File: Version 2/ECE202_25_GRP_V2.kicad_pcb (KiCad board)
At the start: 2 copper layers, 90.2 x 55.1 mm, 27 parts, among them J1 Run_in+, J10 Reverse_in+, J11 ground_in, J12 LED_Low_V+, J2 Brake_in+, J3 Turn_in+, J4 Run_out+, J5 Reverse_Out, J6 Turn_out+, J7 ground_out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

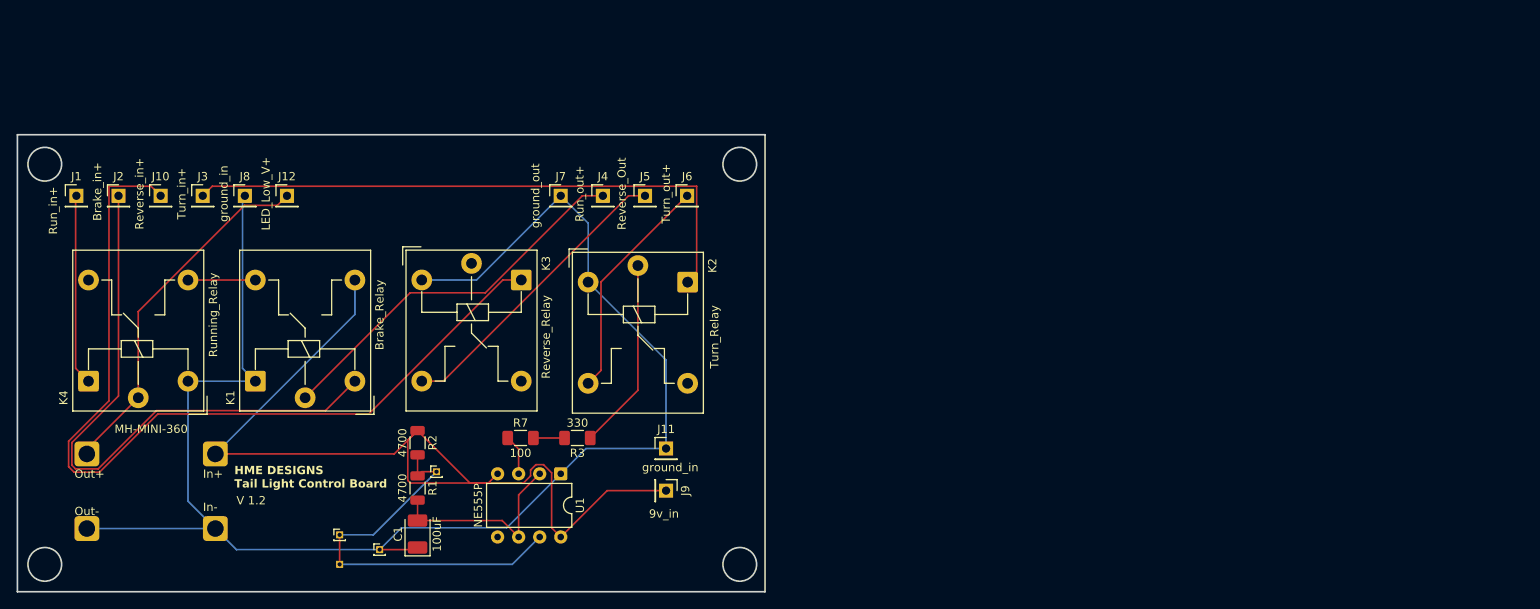
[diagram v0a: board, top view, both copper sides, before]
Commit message: LED Board, practice board, button board updates
Created led board and practice board/business card. Updated mounting for buttons on button board. Submitted all 3 for production on 4/6/25
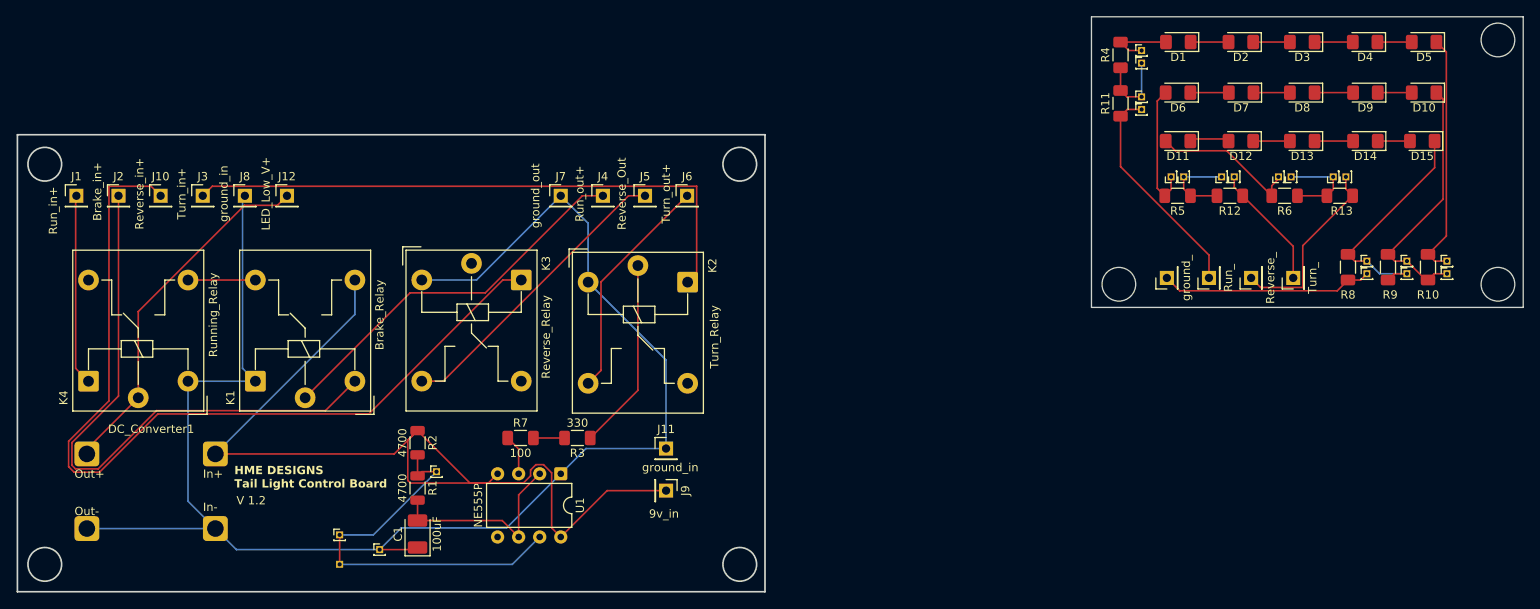
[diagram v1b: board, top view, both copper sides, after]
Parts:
- added D1: LED, LED_SMD:LED_1206_3216Metric_Pad1.42x1.75mm_HandSolder, F.Cu at (228.1, 28.4)
- added D10: LED, LED_SMD:LED_1206_3216Metric_Pad1.42x1.75mm_HandSolder, F.Cu at (257.8, 34.5)
- added D11: LED, LED_SMD:LED_1206_3216Metric_Pad1.42x1.75mm_HandSolder, F.Cu at (228.1, 40.4)
- added D12: LED, LED_SMD:LED_1206_3216Metric_Pad1.42x1.75mm_HandSolder, F.Cu at (235.7, 40.4)
- added D13: LED, LED_SMD:LED_1206_3216Metric_Pad1.42x1.75mm_HandSolder, F.Cu at (243.1, 40.4)
- added D14: LED, LED_SMD:LED_1206_3216Metric_Pad1.42x1.75mm_HandSolder, F.Cu at (250.7, 40.4)
- added D15: LED, LED_SMD:LED_1206_3216Metric_Pad1.42x1.75mm_HandSolder, F.Cu at (257.6, 40.4)
- added D2: LED, LED_SMD:LED_1206_3216Metric_Pad1.42x1.75mm_HandSolder, F.Cu at (235.7, 28.4)
- added D3: LED, LED_SMD:LED_1206_3216Metric_Pad1.42x1.75mm_HandSolder, F.Cu at (243.1, 28.4)
- added D4: LED, LED_SMD:LED_1206_3216Metric_Pad1.42x1.75mm_HandSolder, F.Cu at (250.7, 28.4)
- added D5: LED, LED_SMD:LED_1206_3216Metric_Pad1.42x1.75mm_HandSolder, F.Cu at (257.8, 28.4)
- added D6: LED, LED_SMD:LED_1206_3216Metric_Pad1.42x1.75mm_HandSolder, F.Cu at (228.1, 34.5)
- added D7: LED, LED_SMD:LED_1206_3216Metric_Pad1.42x1.75mm_HandSolder, F.Cu at (235.7, 34.5)
- added D8: LED, LED_SMD:LED_1206_3216Metric_Pad1.42x1.75mm_HandSolder, F.Cu at (243.1, 34.5)
- added D9: LED, LED_SMD:LED_1206_3216Metric_Pad1.42x1.75mm_HandSolder, F.Cu at (250.7, 34.5)
- added J13: Run_, Connector_PinHeader_2.54mm:PinHeader_1x01_P2.54mm_Vertical, F.Cu at (231.8, 56.9)
- added J14: Turn_, Connector_PinHeader_2.54mm:PinHeader_1x01_P2.54mm_Vertical, F.Cu at (242.0, 56.9)
- added J15: Reverse_, Connector_PinHeader_2.54mm:PinHeader_1x01_P2.54mm_Vertical, F.Cu at (236.9, 56.9)
- added J16: ground_, Connector_PinHeader_2.54mm:PinHeader_1x01_P2.54mm_Vertical, F.Cu at (226.8, 56.9)
- added R10: 330, Resistor_SMD:R_1206_3216Metric_Pad1.30x1.75mm_HandSolder, F.Cu at (258.3, 55.6)
- added R11: 330, Resistor_SMD:R_1206_3216Metric_Pad1.30x1.75mm_HandSolder, F.Cu at (221.2, 35.8)
- added R12: 330, Resistor_SMD:R_1206_3216Metric_Pad1.30x1.75mm_HandSolder, F.Cu at (234.4, 47.0)
- added R13: 330, Resistor_SMD:R_1206_3216Metric_Pad1.30x1.75mm_HandSolder, F.Cu at (247.6, 47.0)
- added R4: 330, Resistor_SMD:R_1206_3216Metric_Pad1.30x1.75mm_HandSolder, F.Cu at (221.2, 30.0)
- added R5: 330, Resistor_SMD:R_1206_3216Metric_Pad1.30x1.75mm_HandSolder, F.Cu at (228.1, 47.0)
- added R6: 330, Resistor_SMD:R_1206_3216Metric_Pad1.30x1.75mm_HandSolder, F.Cu at (241.0, 47.0)
- added R8: 330, Resistor_SMD:R_1206_3216Metric_Pad1.30x1.75mm_HandSolder, F.Cu at (248.6, 55.6)
- added R9: 330, Resistor_SMD:R_1206_3216Metric_Pad1.30x1.75mm_HandSolder, F.Cu at (253.4, 55.6)
- added REF**: PinHeader_1x01_P1.00mm_Vertical, Connector_PinHeader_1.00mm:PinHeader_1x01_P1.00mm_Vertical, F.Cu at (255.7, 54.9)
- added REF**: PinHeader_1x01_P1.00mm_Vertical, Connector_PinHeader_1.00mm:PinHeader_1x01_P1.00mm_Vertical, F.Cu at (248.4, 44.7)
- added REF**: PinHeader_1x01_P1.00mm_Vertical, Connector_PinHeader_1.00mm:PinHeader_1x01_P1.00mm_Vertical, F.Cu at (223.7, 35.1)
- added REF**: PinHeader_1x01_P1.00mm_Vertical, Connector_PinHeader_1.00mm:PinHeader_1x01_P1.00mm_Vertical, F.Cu at (234.9, 44.7)
- added REF**: PinHeader_1x01_P1.00mm_Vertical, Connector_PinHeader_1.00mm:PinHeader_1x01_P1.00mm_Vertical, F.Cu at (223.7, 36.6)
- added REF**: PinHeader_1x01_P1.00mm_Vertical, Connector_PinHeader_1.00mm:PinHeader_1x01_P1.00mm_Vertical, F.Cu at (246.8, 44.7)
- added REF**: PinHeader_1x01_P1.00mm_Vertical, Connector_PinHeader_1.00mm:PinHeader_1x01_P1.00mm_Vertical, F.Cu at (260.6, 56.4)
- added REF**: PinHeader_1x01_P1.00mm_Vertical, Connector_PinHeader_1.00mm:PinHeader_1x01_P1.00mm_Vertical, F.Cu at (255.7, 56.4)
- added REF**: PinHeader_1x01_P1.00mm_Vertical, Connector_PinHeader_1.00mm:PinHeader_1x01_P1.00mm_Vertical, F.Cu at (240.2, 44.7)
- added REF**: PinHeader_1x01_P1.00mm_Vertical, Connector_PinHeader_1.00mm:PinHeader_1x01_P1.00mm_Vertical, F.Cu at (223.7, 31.0)
- added REF**: PinHeader_1x01_P1.00mm_Vertical, Connector_PinHeader_1.00mm:PinHeader_1x01_P1.00mm_Vertical, F.Cu at (260.6, 54.9)
- added REF**: PinHeader_1x01_P1.00mm_Vertical, Connector_PinHeader_1.00mm:PinHeader_1x01_P1.00mm_Vertical, F.Cu at (250.9, 56.4)
- added REF**: PinHeader_1x01_P1.00mm_Vertical, Connector_PinHeader_1.00mm:PinHeader_1x01_P1.00mm_Vertical, F.Cu at (250.9, 54.9)
- added REF**: PinHeader_1x01_P1.00mm_Vertical, Connector_PinHeader_1.00mm:PinHeader_1x01_P1.00mm_Vertical, F.Cu at (228.8, 44.7)
- added REF**: PinHeader_1x01_P1.00mm_Vertical, Connector_PinHeader_1.00mm:PinHeader_1x01_P1.00mm_Vertical, F.Cu at (223.7, 29.5)
- added REF**: PinHeader_1x01_P1.00mm_Vertical, Connector_PinHeader_1.00mm:PinHeader_1x01_P1.00mm_Vertical, F.Cu at (233.4, 44.7)
- added REF**: PinHeader_1x01_P1.00mm_Vertical, Connector_PinHeader_1.00mm:PinHeader_1x01_P1.00mm_Vertical, F.Cu at (241.8, 44.7)
- added REF**: PinHeader_1x01_P1.00mm_Vertical, Connector_PinHeader_1.00mm:PinHeader_1x01_P1.00mm_Vertical, F.Cu at (227.3, 44.7)
- renumbered MH-MINI-360 to DC_Converter1
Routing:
- net Net-(D10-K): track 0.00 -> 31.3 mm
- net Net-(D5-K): track 0.00 -> 29.6 mm
- net Net-(D15-K): track 0.00 -> 29.1 mm
- net Net-(J13-Pin_1): track 0.00 -> 26.8 mm
- net Net-(J16-Pin_1): track 0.00 -> 25.6 mm
- net Net-(J15-Pin_1): track 0.00 -> 22.9 mm
- net Net-(D11-A): track 0.00 -> 18.2 mm
- net Net-(D6-A): track 0.00 -> 15.8 mm
- net Net-(J14-Pin_1): track 0.00 -> 15.1 mm
- net Net-(R13-Pad2): track 0.00 -> 11.2 mm
- net Net-(R11-Pad2): track 0.00 -> 10.5 mm
- net Net-(R12-Pad2): track 0.00 -> 10.4 mm
- net Net-(D1-A): track 0.00 -> 8.44 mm
- net Net-(D11-K): track 0.00 -> 4.71 mm
- net Net-(D8-K): track 0.00 -> 4.65 mm
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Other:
- board size 90.2 x 55.1 mm -> 181.6 x 69.3 mm
